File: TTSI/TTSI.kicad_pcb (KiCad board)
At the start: 2 copper layers, 71 x 46 mm, 37 parts, among them Q101 NMOS, Q102 NMOS, Q103 NMOS, Q104 PMOS, Q105 NMOS, Q106 NMOS, U101 641964-1, U102 641964-1, U103 R-78E5.0-0.5, U104 74AHC1G32, U105 641964-1, U106 74AHC1G08, U107 LM555xM, U108 641964-1

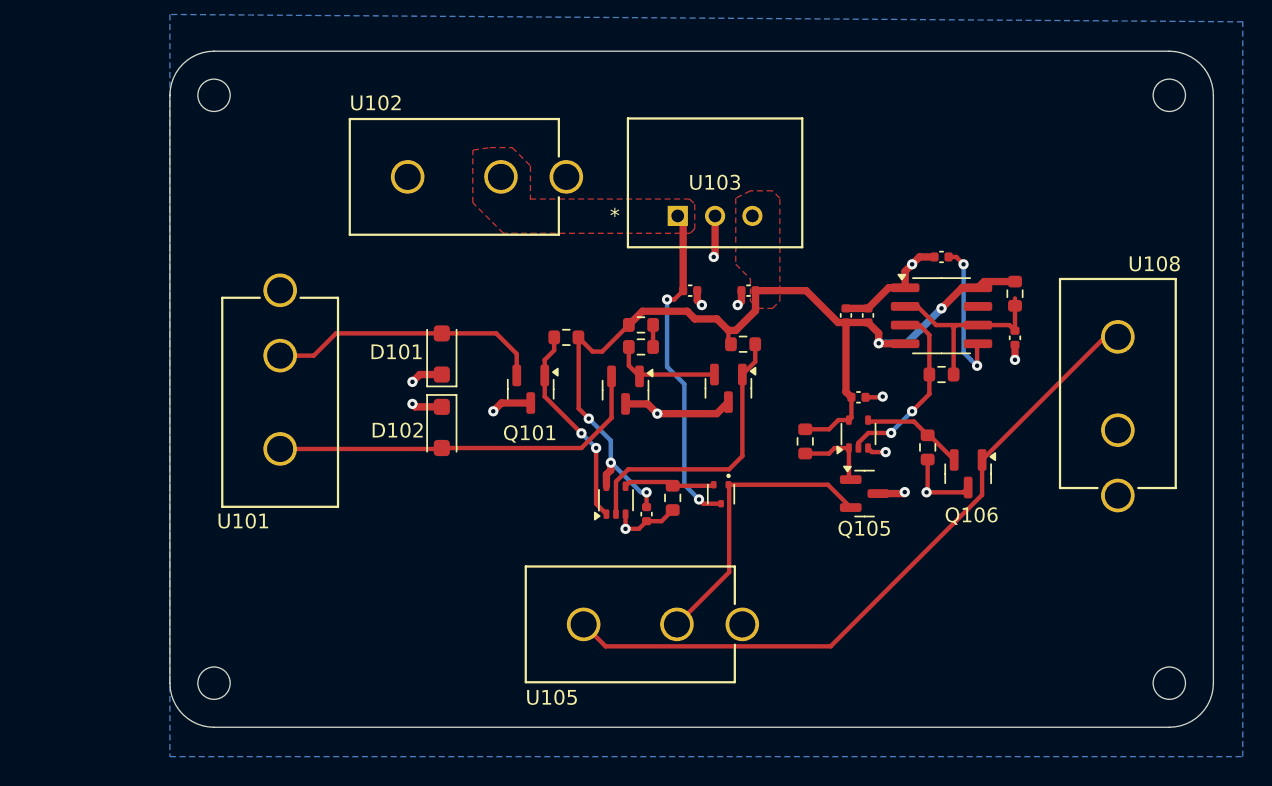
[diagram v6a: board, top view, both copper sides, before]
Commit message: Fixed TSSI footprint issues
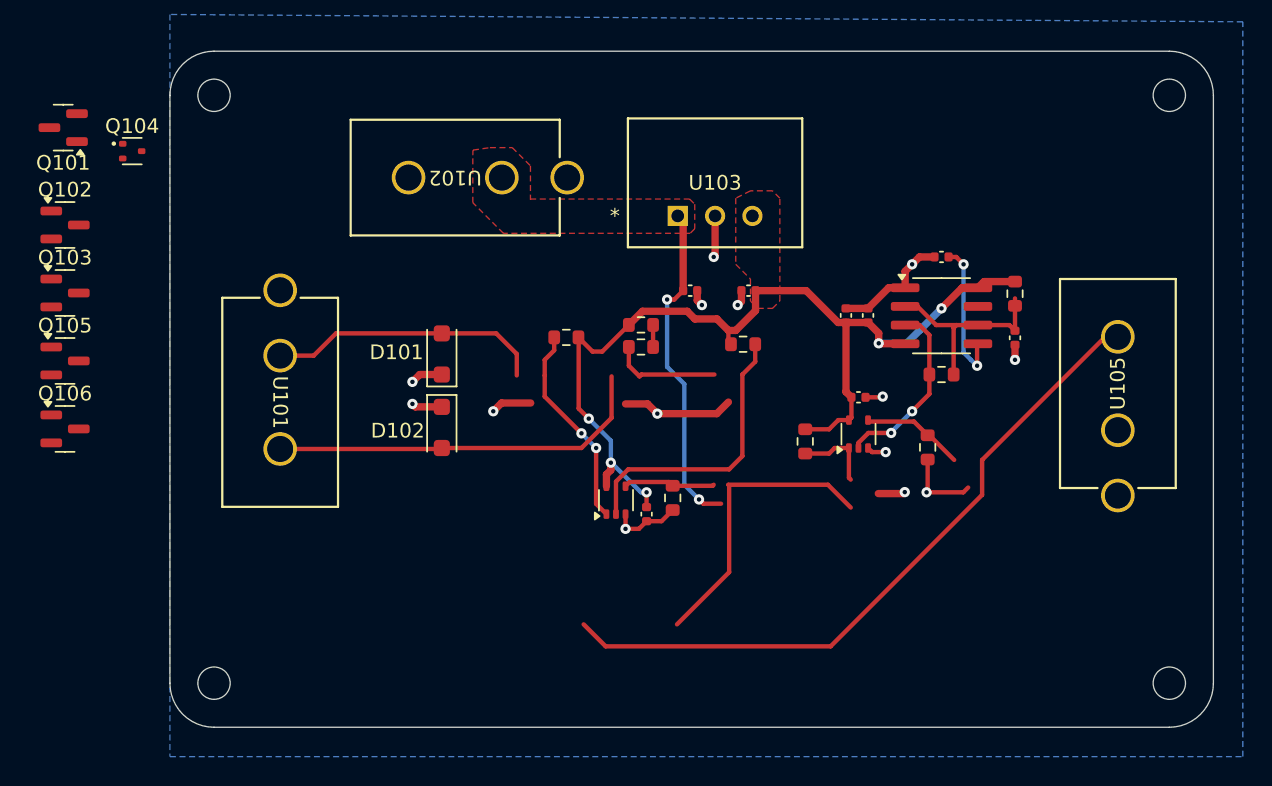
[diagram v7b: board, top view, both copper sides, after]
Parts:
- removed U108: 641964-1, 641964-1:641964-1_TYC
- Q101, Q102, Q103, Q105, Q106: value NMOS -> Q_NMOS_GSD
- Q104: value PMOS -> Q_PMOS_GSD
- U101, U102, U105: footprint 641964-1:641964-1_TYC -> CONNECTOR:641964-1_TYC
- moved Q106 61.5 mm to (114.9, 107.7), turned to 0 degrees
- moved Q105 55.1 mm to (114.9, 103.1)
- moved Q104 46.4 mm to (119.4, 88.8), turned to 0 degrees
- moved Q103 45.6 mm to (114.9, 98.5), turned to 0 degrees
- moved Q102 39.8 mm to (114.9, 93.8), turned to 0 degrees
- moved Q101 36.5 mm to (114.7, 87.2), turned to 180 degrees
- moved U105 32.8 mm to (186.5, 107.8), turned to 90 degrees
- moved U102 0.08 mm to (144.6, 90.6)
- renumbered H1 to H101, H2 to H102, H3 to H103, H4 to H104
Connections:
- Q101 pad 1: /BMS_LV -> BMS_HV
- Q101 pad 2: BMS_HV -> GND
- Q101 pad 3: GND -> /BMS_LV
- Q102 pad 1: Net-(D103-K) -> IMD_HV
- Q102 pad 2: IMD_HV -> GND
- Q102 pad 3: GND -> Net-(D103-K)
- Q103 pad 1: /IMD_LV -> Net-(D103-K)
- Q103 pad 2: Net-(D103-K) -> GND
- Q103 pad 3: GND -> /IMD_LV
- Q104 pad 1: Net-(Q104-D) -> Net-(Q104-G)
- Q104 pad 2: Net-(Q104-G) -> Net-(Q104-S)
- Q105 pad 1: Net-(Q105-D) -> Net-(Q104-S)
- Q105 pad 2: Net-(Q104-D) -> GND
- Q105 pad 3: GND -> Net-(Q105-D)
- Q106 pad 1: Net-(Q106-D) -> Net-(Q106-G)
- Q106 pad 2: Net-(Q106-G) -> GND
- Q106 pad 3: GND -> Net-(Q106-D)
- U105 pad 1: Net-(Q104-D) -> Net-(Q104-S)
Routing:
- net Net-(Q104-S): track 0.00 -> 20.0 mm
- net Net-(Q104-D): track 20.0 -> 0.00 mm

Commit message: redid tssi layout
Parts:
- moved Q106 61.7 mm to (176.5, 110.9)
- moved Q105 54.1 mm to (168.2, 111.9), turned to 90 degrees
- moved Q104 47.6 mm to (160.6, 112.8)
- moved Q103 45.8 mm to (160.2, 105.1)
- moved Q102 41.1 mm to (154.2, 105.8)
- moved Q101 36.6 mm to (146.8, 104.9), turned to 0 degrees
- moved D103 1.40 mm to (155.3, 102.8)
- moved R102 1.35 mm to (155.3, 101.2)
- moved R103 0.10 mm to (160.9, 101.9)
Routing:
- net Net-(Q106-D): track 47.1 -> 13.7 mm
- net Net-(Q104-S): track 20.0 -> 31.9 mm
- net GND: track 43.3 -> 35.9 mm, vias 14 -> 13
- net +12V: track 22.7 -> 26.7 mm
- net Net-(Q104-G): track 6.25 -> 7.48 mm
- net +5V: track 65.7 -> 64.7 mm
- net Net-(D103-K): track 7.45 -> 8.35 mm
- net /THRESH: track 13.8 -> 13.1 mm
